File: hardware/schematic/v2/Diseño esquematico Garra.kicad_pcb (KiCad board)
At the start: 2 copper layers, 85.5 x 137 mm, 18 parts

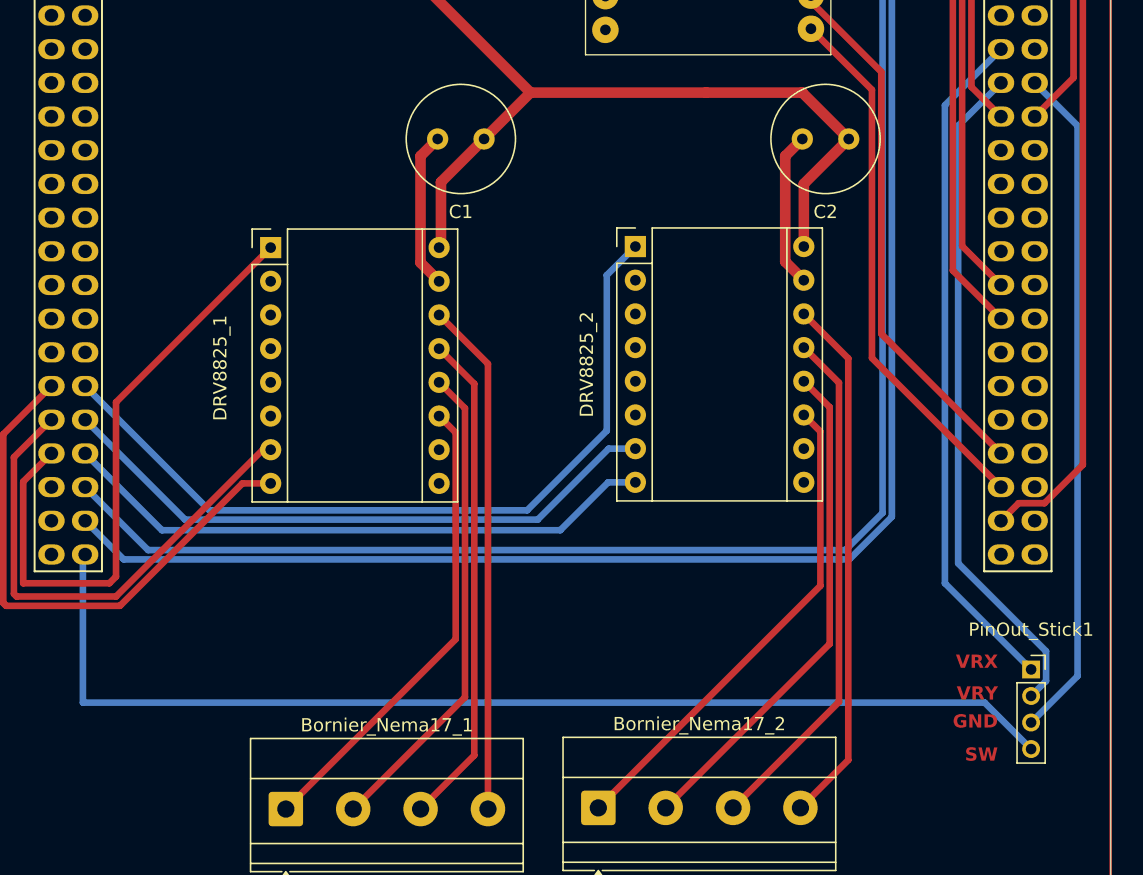
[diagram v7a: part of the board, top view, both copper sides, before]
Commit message: docs: Schematics PDF added
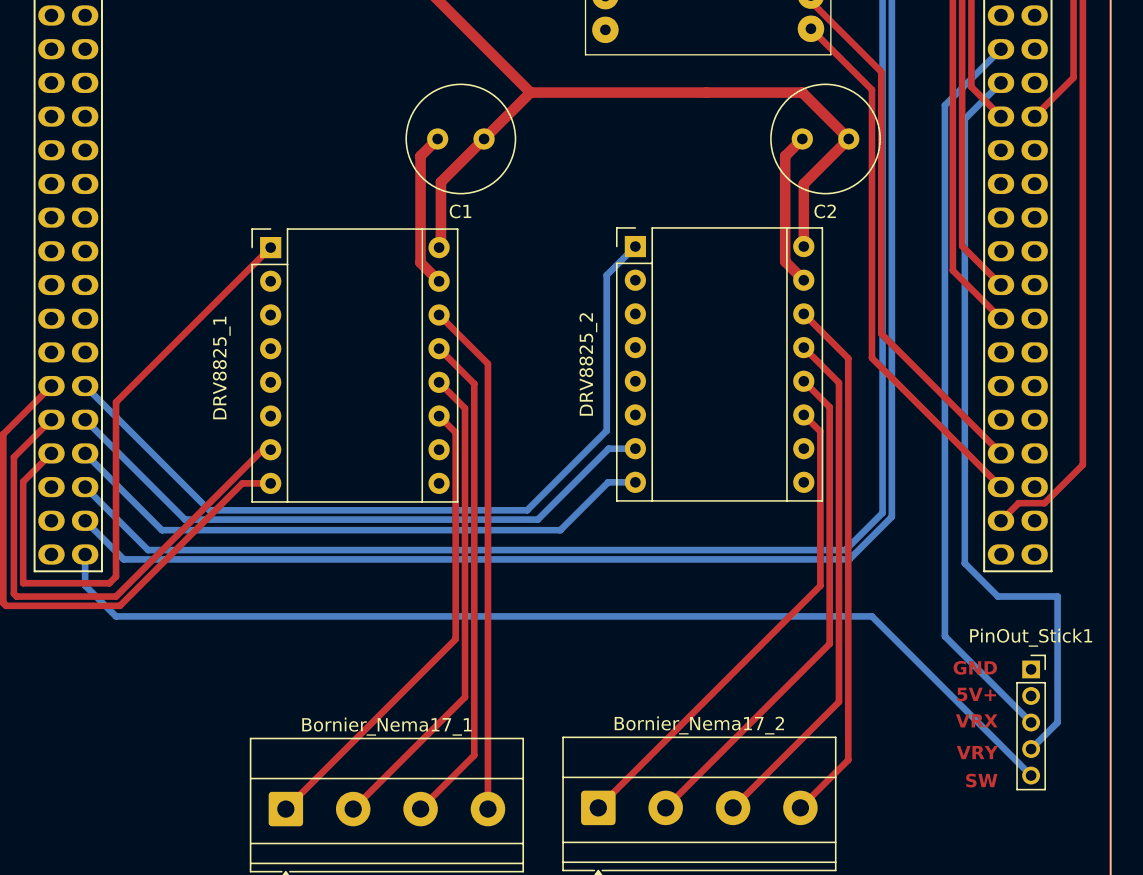
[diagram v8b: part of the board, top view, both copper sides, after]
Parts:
- PinOut_Stick1: footprint Connector_PinSocket_2.00mm:PinSocket_1x04_P2.00mm_Vertical -> Connector_PinSocket_2.00mm:PinSocket_1x05_P2.00mm_Vertical
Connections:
- PinOut_Stick1 pad 1: VRX -> GND_Stick
- PinOut_Stick1 pad 2: VRY -> 5V
- PinOut_Stick1 pad 3: GND_Stick -> VRX
- PinOut_Stick1 pad 4: SW -> VRY
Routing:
- net GND_Stick: track 51.0 -> 0.00 mm
- net VRY: track 50.8 -> 57.7 mm
- net SW: track 84.2 -> 79.8 mm
- net VRX: track 51.2 -> 55.2 mm
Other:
- board text added: "5V+"
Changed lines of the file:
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@@
 	(net 87 "unconnected-(DRV8825_1-~{FLT}-Pad10)")
 	(net 88 "unconnected-(DRV8825_2-~{FLT}-Pad10)")
-	(footprint "Connector_PinSocket_2.00mm:PinSocket_1x04_P2.00mm_Vertical"
+	(footprint "Connector_PinSocket_2.00mm:PinSocket_1x05_P2.00mm_Vertical"
 		(layer "F.Cu")
 		(at 114.5 144)
-		(descr "Through hole straight socket strip, 1x04, 2.00mm pitch, single row (from Kicad 4.0.7), script generated")
-		(tags "Through hole socket strip THT 1x04 2.00mm single row")
+		(descr "Through hole straight socket strip, 1x05, 2.00mm pitch, single row (from Kicad 4.0.7), script generated")
+		(tags "Through hole socket strip THT 1x05 2.00mm single row")
 		(property "Reference" "PinOut_Stick1"
-			(at 0 -3 0)
+			(at 0 -2.5 0)
 			(layer "F.SilkS")
 			(effects
@@
 		)
 		(property "Value" "Pin_Terminal_01x05"
-			(at 0 8.5 0)
+			(at 0 10.5 0)
 			(layer "F.Fab")
-			(hide yes)
 			(effects
 				(font
@@
 		(fp_line
 			(start -1.06 1)
-			(end -1.06 7.06)
+			(end -1.06 9.06)
 			(stroke
 				(width 0.12)
@@
 		)
 		(fp_line
-			(start -1.06 7.06)
-			(end 1.06 7.06)
+			(start -1.06 9.06)
+			(end 1.06 9.06)
 			(stroke
 				(width 0.12)
@@
 		(fp_line
 			(start 1.06 1)
-			(end 1.06 7.06)
+			(end 1.06 9.06)
 			(stroke
 				(width 0.12)
@@
 		)
 		(fp_line
-			(start -1.5 7.5)
+			(start -1.5 9.5)
 			(end -1.5 -1.5)
 			(stroke
@@
 		(fp_line
 			(start 1.5 -1.5)
-			(end 1.5 7.5)
+			(end 1.5 9.5)
 			(stroke
 				(width 0.05)
@@
 		)
 		(fp_line
-			(start 1.5 7.5)
-			(end -1.5 7.5)
+			(start 1.5 9.5)
+			(end -1.5 9.5)
 			(stroke
 				(width 0.05)
@@
 		)
 		(fp_line
-			(start -1 7)
+			(start -1 9)
 			(end -1 -1)
 			(stroke
@@
 		(fp_line
 			(start 1 -0.5)
-			(end 1 7)
+			(end 1 9)
 			(stroke
 				(width 0.1)
@@
 		)
 		(fp_line
-			(start 1 7)
-			(end -1 7)
+			(start 1 9)
+			(end -1 9)
 			(stroke
 				(width 0.1)
@@
 			(layer "F.Fab")
 		)
+		(fp_text user "${REFERENCE}"
+			(at 0 4 90)
+			(layer "F.Fab")
+			(effects
+				(font
+					(size 1 1)
+					(thickness 0.15)
+				)
+			)
+		)
 		(pad "1" thru_hole rect
 			(at 0 0)
@@
 			(layers "*.Cu" "*.Mask")
 			(remove_unused_layers no)
-			(net 17 "VRX")
+			(net 21 "GND_Stick")
 			(pinfunction "Pin_1")
 			(pintype "passive")
@@
 			(layers "*.Cu" "*.Mask")
 			(remove_unused_layers no)
-			(net 20 "VRY")
+			(net 11 "5V")
 			(pinfunction "Pin_2")
 			(pintype "passive")
@@
 			(layers "*.Cu" "*.Mask")
 			(remove_unused_layers no)
-			(net 21 "GND_Stick")
+			(net 17 "VRX")
 			(pinfunction "Pin_3")
 			(pintype "passive")
@@
 			(layers "*.Cu" "*.Mask")
 			(remove_unused_layers no)
-			(net 86 "SW")
+			(net 20 "VRY")
 			(pinfunction "Pin_4")
 			(pintype "passive")
 		)
+		(pad "5" thru_hole circle
+			(at 0 8)
+			(size 1.35 1.35)
+			(drill 0.8)
+			(layers "*.Cu" "*.Mask")
+			(remove_unused_layers no)
+			(net 86 "SW")
+			(pinfunction "Pin_5")
+			(pintype "passive")
+		)
 		(embedded_fonts no)
-		(model "${KICAD9_3DMODEL_DIR}/Connector_PinSocket_2.00mm.3dshapes/PinSocket_1x04_P2.00mm_Vertical.step"
+		(model "${KICAD9_3DMODEL_DIR}/Connector_PinSocket_2.00mm.3dshapes/PinSocket_1x05_P2.00mm_Vertical.step"
 			(offset
 				(xyz 0 0 0)
@@
 	)
 	(gr_text "VRY\n\n"
-		(at 112 148 0)
+		(at 112 152.5 0)
 		(layer "F.Cu")
 		(effects
@@
 	)
 	(gr_text "GND"
-		(at 112 148.5 0)
+		(at 112 144.5 0)
+		(layer "F.Cu")
+		(effects
+			(font
+				(size 1 1)
+				(thickness 0.2)
+				(bold yes)
+			)
+			(justify right bottom)
+		)
+	)
+	(gr_text "5V+\n"
+		(at 112 146.5 0)
 		(layer "F.Cu")
 		(effects
@@
 	)
 	(gr_text "SW"
-		(at 112 151 0)
+		(at 112 153 0)
 		(layer "F.Cu")
 		(effects
@@
 	)
 	(gr_text "VRX\n"
-		(at 112 144 0)
+		(at 112 148.5 0)
 		(layer "F.Cu")
 		(effects
@@
 	)
 	(segment
-		(start 108 137.5)
-		(end 108 101.46)
+		(start 108 101.46)
+		(end 112.23 97.23)
 		(width 0.5)
 		(layer "B.Cu")
@@
 	)
 	(segment
-		(start 108 101.46)
-		(end 112.23 97.23)
+		(start 114.5 148)
+		(end 108 141.5)
 		(width 0.5)
 		(layer "B.Cu")
@@
 	)
 	(segment
-		(start 114.5 144)
-		(end 108 137.5)
+		(start 108 141.5)
+		(end 108 101.46)
 		(width 0.5)
 		(layer "B.Cu")
@@
 	)
 	(segment
-		(start 115.626 142.626)
-		(end 109 136)
-		(width 0.5)
-		(layer "B.Cu")
-		(net 20)
-	)
-	(segment
-		(start 109 103)
+		(start 109.5 102.5)
 		(end 112.23 99.77)
 		(width 0.5)
@@
 	)
 	(segment
-		(start 109 136)
-		(end 109 103)
+		(start 116.5 138.5)
+		(end 112 138.5)
 		(width 0.5)
 		(layer "B.Cu")
@@
 	)
 	(segment
-		(start 115.626 144.874)
-		(end 115.626 142.626)
+		(start 109.5 136)
+		(end 109.5 102.5)
 		(width 0.5)
 		(layer "B.Cu")
@@
 	)
 	(segment
-		(start 114.5 146)
-		(end 115.626 144.874)
+		(start 114.5 150)
+		(end 116.5 148)
 		(width 0.5)
 		(layer "B.Cu")
@@
 	)
 	(segment
-		(start 114.5 148)
-		(end 118 144.5)
-		(width 0.5)
-		(layer "B.Cu")
-		(net 21)
-	)
-	(segment
-		(start 118 103)
-		(end 114.77 99.77)
+		(start 116.5 148)
+		(end 116.5 138.5)
 		(width 0.5)
 		(layer "B.Cu")
-		(net 21)
+		(net 20)
 	)
 	(segment
-		(start 118 144.5)
-		(end 118 103)
+		(start 112 138.5)
+		(end 109.5 136)
 		(width 0.5)
 		(layer "B.Cu")
-		(net 21)
+		(net 20)
 	)
 	(segment
@@
 	)
 	(segment
-		(start 111 146.5)
-		(end 114.5 150)
+		(start 102.5 140)
+		(end 45.5 140)
 		(width 0.5)
 		(layer "B.Cu")
@@
 	)
 	(segment
-		(start 43 135.5)
-		(end 43 146.5)
+		(start 43.17 137.67)
+		(end 43.17 135.33)
 		(width 0.5)
 		(layer "B.Cu")
@@
 	)
 	(segment
-		(start 43.17 135.33)
-		(end 43 135.5)
+		(start 114.5 152)
+		(end 102.5 140)
+		(width 0.5)
+		(layer "B.Cu")
+		(net 86)
+	)
+	(segment
+		(start 45.5 140)
+		(end 43.17 137.67)
 		(width 0.5)
 		(layer "B.Cu")
@@
 	)
 	(segment
-		(start 43 146.5)
-		(end 111 146.5)
+		(start 43.17 135.33)
+		(end 43 135.5)
 		(width 0.5)
 		(layer "B.Cu")
